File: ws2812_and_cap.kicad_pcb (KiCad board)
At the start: 2 copper layers, 2 parts

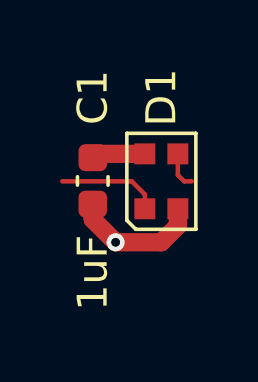
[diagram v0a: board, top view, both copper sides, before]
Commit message: place perim LEDs
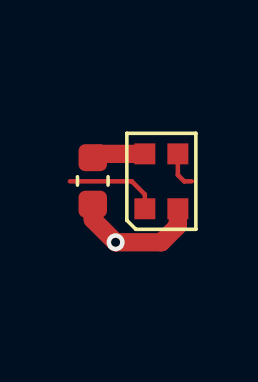
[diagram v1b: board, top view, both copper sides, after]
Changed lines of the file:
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@@
 		(property "Reference" "D1"
 			(at 2.794 0 90)
-			(layer "F.SilkS")
+			(layer "F.Fab")
 			(effects
 				(font
@@
 		(property "Reference" "C1"
 			(at -2.781 0 90)
-			(layer "F.SilkS")
+			(layer "F.Fab")
 			(effects
 				(font
@@
 		(property "Value" "1uF"
 			(at 3.061 0 90)
-			(layer "F.SilkS")
+			(layer "F.Fab")
 			(effects
 				(font
@@
 	(segment
 		(start 151.4135 98.552)
-		(end 149.098 98.552)
+		(end 149.352 98.552)
 		(width 0.1524)
 		(layer "F.Cu")
